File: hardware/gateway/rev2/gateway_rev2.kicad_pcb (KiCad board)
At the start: 2 copper layers, 100 x 45 mm, 80 parts, among them IC1 STM8L151K4T6, IC2 CC1101RGPR, IC3 LT1615ES5-1#TRMPBF, IC4 MIC4427YM, IC5 MB85RC64TAPNF-G-BDERE1, J1 G8250041000YEU, J2 M20-9770342, Q1 IRLML6402TRPBF, U1 2462, Y1 NX3225GA-26.000M-STD-CRG-2

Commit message: EG-59 Schematic with the needed components, plus PCB.
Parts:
- removed ANT1: ANT-433-HESM, MyParts:ANT433HESM
- removed C1, C2: 100nF, Capacitor_SMD:C_0603_1608Metric
- removed C15, C16, C17, C30: 100nF, Capacitor_SMD:C_0402_1005Metric
- removed C18, C19: 12pF, Capacitor_SMD:C_0402_1005Metric
- removed C20, C22: 3.9pF, Capacitor_SMD:C_0402_1005Metric
- removed C21, C25: 220pF, Capacitor_SMD:C_0402_1005Metric
- removed C23: 8.2pF, Capacitor_SMD:C_0402_1005Metric
- removed C24: 5.6pF, Capacitor_SMD:C_0402_1005Metric
- removed C26: 22uF, 6.3V, Capacitor_SMD:C_1206_3216Metric
- removed C27: 4.7pF, Capacitor_SMD:C_0402_1005Metric
- removed C28, C29: 4.7uF, 25V, Capacitor_SMD:C_0805_2012Metric
- removed C6: 47uF, 6.3V, Capacitor_SMD:C_1206_3216Metric
- removed D1: MBR0520LT3G, MyParts:SOD3716X135N
- removed IC3: LT1615ES5-1#TRMPBF, MyParts:SOT95P280X100-5N
- removed IC4: MIC4427YM, MyParts:SOIC127P599X173-8N
- removed J1: G8250041000YEU, MyParts:HDRV4W55P0X200_1X4_800X200X635P
- removed L1, L2, L4: 27nH, Inductor_SMD:L_0402_1005Metric
- removed L3: 22nH, Inductor_SMD:L_0402_1005Metric
- removed L5: CD43NP-100MC, MyParts:CD43NP100MC
- removed Q1: IRLML6402TRPBF, MyParts:SOT95P237X112-3N
- removed R1, R15, R3: 100K, Resistor_SMD:R_0603_1608Metric
- removed R13: 56K, Resistor_SMD:R_0402_1005Metric
- removed R16: 130K, Resistor_SMD:R_0402_1005Metric
- removed R17: 1.15M, Resistor_SMD:R_0402_1005Metric
- removed R2, R5: 1M, Resistor_SMD:R_0603_1608Metric
- removed R4: 10K, Resistor_SMD:R_0603_1608Metric
- removed R6: 510K, Resistor_SMD:R_0603_1608Metric
- removed R7: 1K, Resistor_SMD:R_0603_1608Metric
- removed S1: MASM-14R-8-10, MyParts:MASM14R810
- removed S2: TL6120DF160QG, MyParts:TL6120DF160QG
- added C101: 15pF, Capacitor_SMD:C_0402_1005Metric, F.Cu at (239.9, 118.8)
- added C121: 1pF, Capacitor_SMD:C_0402_1005Metric, F.Cu at (239.9, 120.8)
- added C122: 1.5pF, Capacitor_SMD:C_0402_1005Metric, F.Cu at (239.9, 122.8)
- added C123: 3.3pF, Capacitor_SMD:C_0402_1005Metric, F.Cu at (239.9, 124.8)
- added C124: 100pF, Capacitor_SMD:C_0402_1005Metric, F.Cu at (242.7, 114.9)
- added C125: 12pF, Capacitor_SMD:C_0402_1005Metric, F.Cu at (242.7, 116.9)
- added C131: 1.5pF, Capacitor_SMD:C_0402_1005Metric, F.Cu at (242.7, 118.8)
- added C51: 100nF, Capacitor_SMD:C_0402_1005Metric, F.Cu at (239.9, 114.9)
- added C81: 15pF, Capacitor_SMD:C_0402_1005Metric, F.Cu at (239.9, 116.9)
- added CLK1: SPI_CK, TestPoint:TestPoint_Pad_D1.0mm, F.Cu at (220.1, 111.0)
- added CS1: SPI_CS, TestPoint:TestPoint_Pad_D1.0mm, F.Cu at (220.1, 114.0)
- added GD1: GD0, TestPoint:TestPoint_Pad_D1.0mm, F.Cu at (220.1, 117.1)
- added L121: 12nH, Inductor_SMD:L_0402_1005Metric, F.Cu at (234.1, 114.9)
- added L122: 18nH, Inductor_SMD:L_0402_1005Metric, F.Cu at (234.1, 116.9)
- added L123: 12nH, Inductor_SMD:L_0402_1005Metric, F.Cu at (234.1, 118.9)
- added L124: 12nH, Inductor_SMD:L_0402_1005Metric, F.Cu at (234.1, 120.9)
- added L131: 12nH, Inductor_SMD:L_0402_1005Metric, F.Cu at (234.1, 122.9)
- added L132: 18nH, Inductor_SMD:L_0402_1005Metric, F.Cu at (234.1, 124.9)
- added LED_B1: LED, TestPoint:TestPoint_Pad_D1.0mm, F.Cu at (223.2, 111.0)
- added LED_R1: LED, TestPoint:TestPoint_Pad_D1.0mm, F.Cu at (223.2, 114.0)
- added LED_Y1: LED, TestPoint:TestPoint_Pad_D1.0mm, F.Cu at (223.2, 117.1)
- added MCUVDD1: MCU_VDD, TestPoint:TestPoint_Pad_D1.0mm, F.Cu at (226.2, 111.0)
- added MISO1: SPI_MISO, TestPoint:TestPoint_Pad_D1.0mm, F.Cu at (226.2, 114.0)
- added MOSI1: SPI_MOSI, TestPoint:TestPoint_Pad_D1.0mm, F.Cu at (226.2, 117.1)
- added R171: 56K, Resistor_SMD:R_0402_1005Metric, F.Cu at (234.1, 126.9)
- added RFVDD1: RF_VDD, TestPoint:TestPoint_Pad_D1.0mm, F.Cu at (245.7, 124.3)
- C13: value 1uF -> 100nF
- C9: value 47uF, 6.3V -> 100nF; footprint Capacitor_SMD:C_1206_3216Metric -> Capacitor_SMD:C_0402_1005Metric
- R18, R19: value 33R -> 100R
- R20: value 1M -> 10K
- U1: value 2462 -> IRM-01-3.3; footprint MyParts:2462 -> MyParts:IRM-01-3-3; moved to F.Cu
- Y1: value NX3225GA-26.000M-STD-CRG-2 -> NX3225GA-26MHZ-TI
- moved FID2 84.5 mm to (241.0, 91.0)
- moved H2 82.1 mm to (235.9, 95.5)
- moved FID1 64.3 mm to (241.0, 87.5)
- moved H4 63.8 mm to (235.9, 108.6)
- moved C4 62.7 mm to (224.6, 87.0), turned to 0 degrees
- moved FID3 61.8 mm to (241.0, 94.6)
- moved H1 61.0 mm to (235.9, 89.0)
- moved C5 60.8 mm to (224.6, 89.5), turned to 0 degrees
- moved U1 59.2 mm to (191.5, 154.5)
- moved LS1 54.5 mm to (251.6, 146.1), turned to 0 degrees
- moved R18 51.4 mm to (228.7, 92.0)
- moved R10 50.7 mm to (224.6, 97.0)
- moved LED3 48.3 mm to (225.4, 101.4)
- moved R9 47.6 mm to (224.6, 94.5)
- moved R20 44.9 mm to (228.7, 97.0), turned to 0 degrees
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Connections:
- C11 pad 1: Net-(IC2-DCOUPL) -> RF_VDD
- C9 pad 1: VDD -> RF_VDD
- FB1 pad 1: VDD -> RF_VDD
- FB1 pad 2: RF_VDD -> VDD
- IC1 pad 11: /Buzzer/BZR_P -> BZR_P
- IC1 pad 22: DOOR -> unconnected-(IC1-PD5-Pad22)
- IC1 pad 24: /Buzzer/BZR_N -> BZR_N
- IC1 pad 29: /Buzzer/BZR_EN -> unconnected-(IC1-PC4-Pad29)
- IC1 pad 6: V_MEAS -> unconnected-(IC1-PA6-Pad6)
- J2 pad 1: TX -> GND
- J2 pad 3: GND -> TX
- R18 pad 2: Net-(IC4-OUTA) -> BZR_P
- R19 pad 2: Net-(IC4-OUTB) -> BZR_N
- U1 pad 1: BAT_IN -> unconnected-(U1-AC/L-Pad1)
- Y1 pad 2: GND -> unconnected-(Y1-NC/GND_1-Pad2)
- Y1 pad 4: GND -> unconnected-(Y1-NC/GND_2-Pad4)
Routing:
- net VDD: track 157.1 -> 0.00 mm, vias 5 -> 0
- net GND: track 80.1 -> 0.00 mm, vias 287 -> 0
- net /Buzzer/BZR_EN: track 47.7 -> 0.00 mm, vias 2 -> 0
- net RF_VDD: track 47.6 -> 0.00 mm, vias 4 -> 0
- net /MCU/SDI: track 45.8 -> 0.00 mm, vias 4 -> 0
- net /MCU/SDO: track 40.2 -> 0.00 mm, vias 4 -> 0
- net RX: track 39.2 -> 0.00 mm, vias 1 -> 0
- net /MCU/SCLK: track 36.0 -> 0.00 mm, vias 4 -> 0
- net TX: track 35.8 -> 0.00 mm, vias 2 -> 0
- net +12V: track 34.3 -> 0.00 mm, vias 2 -> 0
- net SCL: track 33.5 -> 0.00 mm, vias 2 -> 0
- net SDA: track 32.1 -> 0.00 mm, vias 2 -> 0
- net /MCU/CS: track 31.4 -> 0.00 mm, vias 2 -> 0
- net /MCU/IRQ: track 30.5 -> 0.00 mm, vias 2 -> 0
- net LED_B: track 28.9 -> 0.00 mm, vias 2 -> 0
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- removed copper zone on B.Cu, net GND
- removed copper zone on F.Cu, net GND
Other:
- board size 100 x 45 mm -> 94 x 78 mm
- board text removed: "Exit Guardian - Gateway REV1.0 NPX4U 2025"

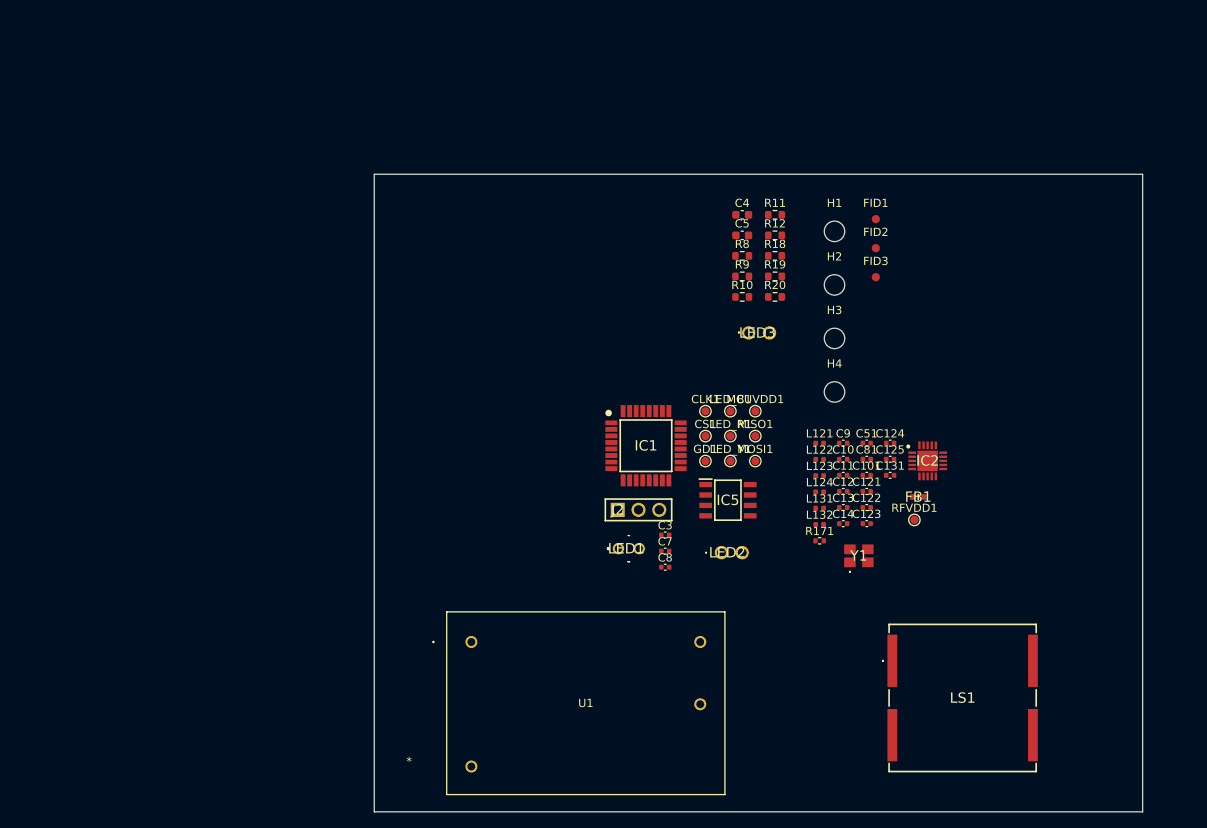
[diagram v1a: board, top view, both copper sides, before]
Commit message: EG-59 First mechanical project with the AC-DC component and buzzer.
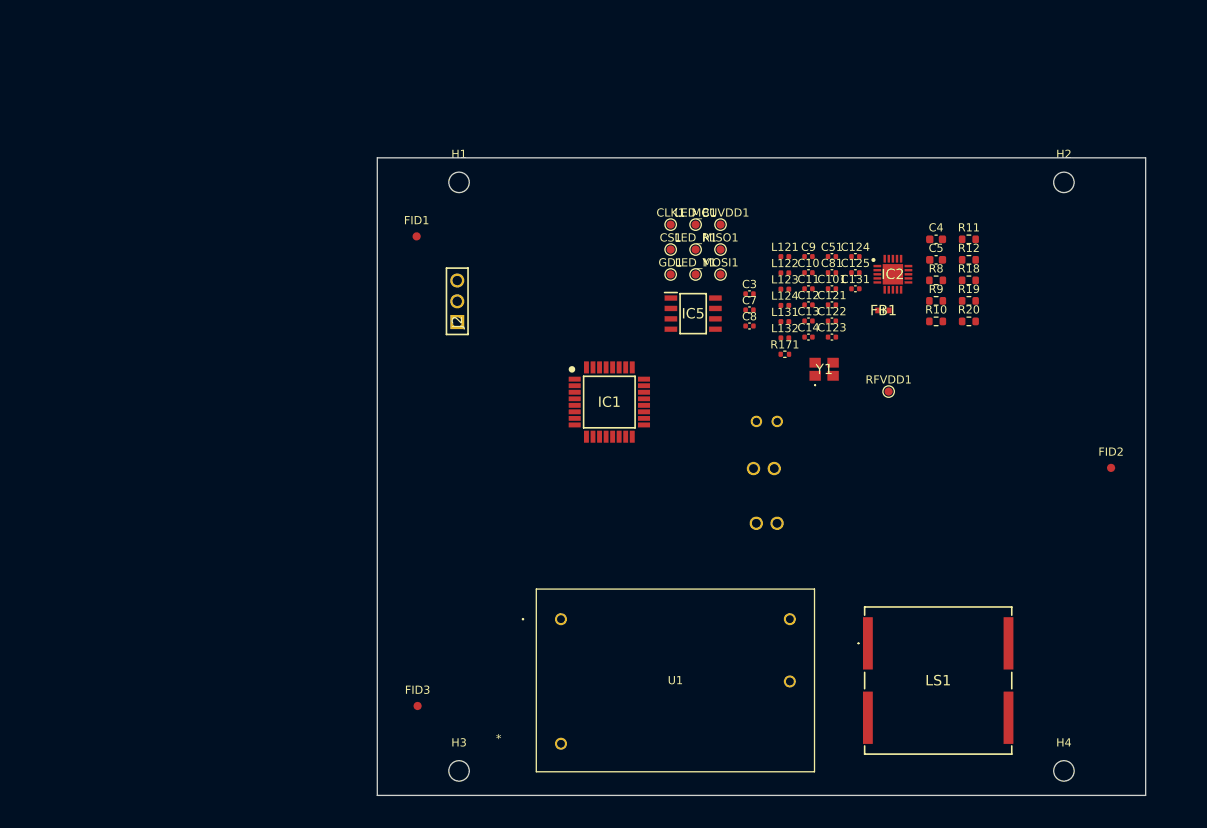
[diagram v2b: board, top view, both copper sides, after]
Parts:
- LED1, LED2, LED3: moved to B.Cu
- moved FID3 76.8 mm to (184.9, 147.1)
- moved H3 70.1 mm to (190.0, 155.0)
- moved FID1 56.2 mm to (184.8, 89.6)
- moved H4 54.2 mm to (264.0, 155.0)
- moved H1 46.3 mm to (190.0, 83.0)
- moved FID2 39.4 mm to (269.8, 117.9)
- moved C7 31.3 mm to (225.5, 98.6)
- moved C8 31.3 mm to (225.5, 100.6)
- moved C3 31.3 mm to (225.5, 96.6)
- moved H2 30.7 mm to (264.0, 83.0)
- moved J2 30.2 mm to (189.8, 100.1), turned to 90 degrees
- moved LED1 24.9 mm to (228.9, 112.2), turned to 180 degrees
- moved C4 23.9 mm to (248.4, 90.0)
- moved C5 23.9 mm to (248.4, 92.5)
- moved R10 23.9 mm to (248.4, 100.0)
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
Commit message: EG-59 Correct position of AC-DC and buzzer in the PCB.
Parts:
- added TP1: TestPoint, TestPoint:TestPoint_Plated_Hole_D2.0mm, F.Cu at (190.0, 133.0)
- added TP2: TestPoint, TestPoint:TestPoint_Plated_Hole_D2.0mm, F.Cu at (190.0, 147.0)
- moved FID1 13.5 mm to (196.5, 83.0)
- moved FID3 8.03 mm to (183.6, 155.0)
- moved LS1 4.13 mm to (249.9, 140.0), turned to 90 degrees
- moved U1 3.93 mm to (201.9, 147.8)
- moved FID2 2.29 mm to (270.8, 120.0)
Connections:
- U1 pad 1: unconnected-(U1-AC/L-Pad1) -> Net-(U1-AC/L)
- U1 pad 12: unconnected-(U1-+VO-Pad12) -> VDD
- U1 pad 13: unconnected-(U1--VO-Pad13) -> GND
- U1 pad 24: unconnected-(U1-AC/N-Pad24) -> Net-(U1-AC/N)
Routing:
- net Net-(U1-AC/L): track 0.00 -> 12.2 mm
- net Net-(U1-AC/N): track 0.00 -> 12.1 mm
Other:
- board text added: "Exit Guardian - Gateway REV2.0 NPX4U 2026"

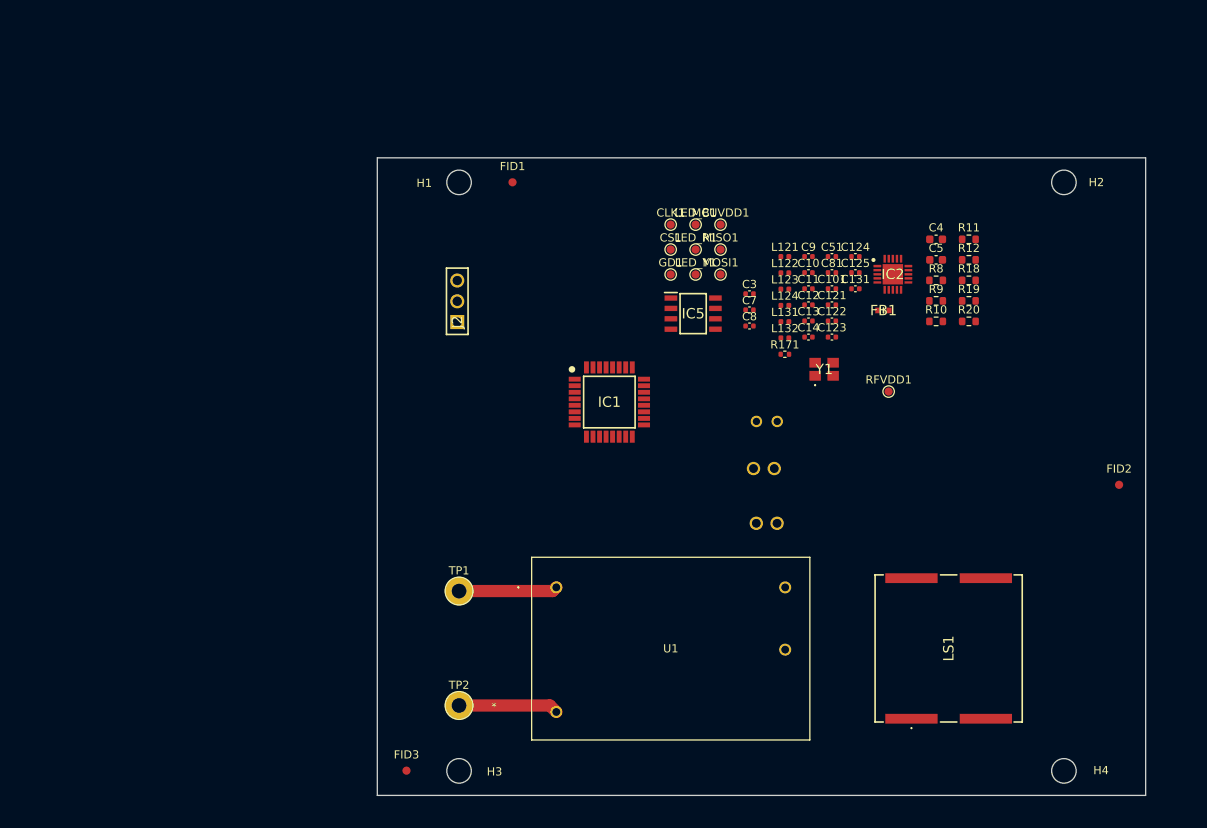
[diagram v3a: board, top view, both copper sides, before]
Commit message: EG-59 Antenna and headers fix, from schematic to 3D.
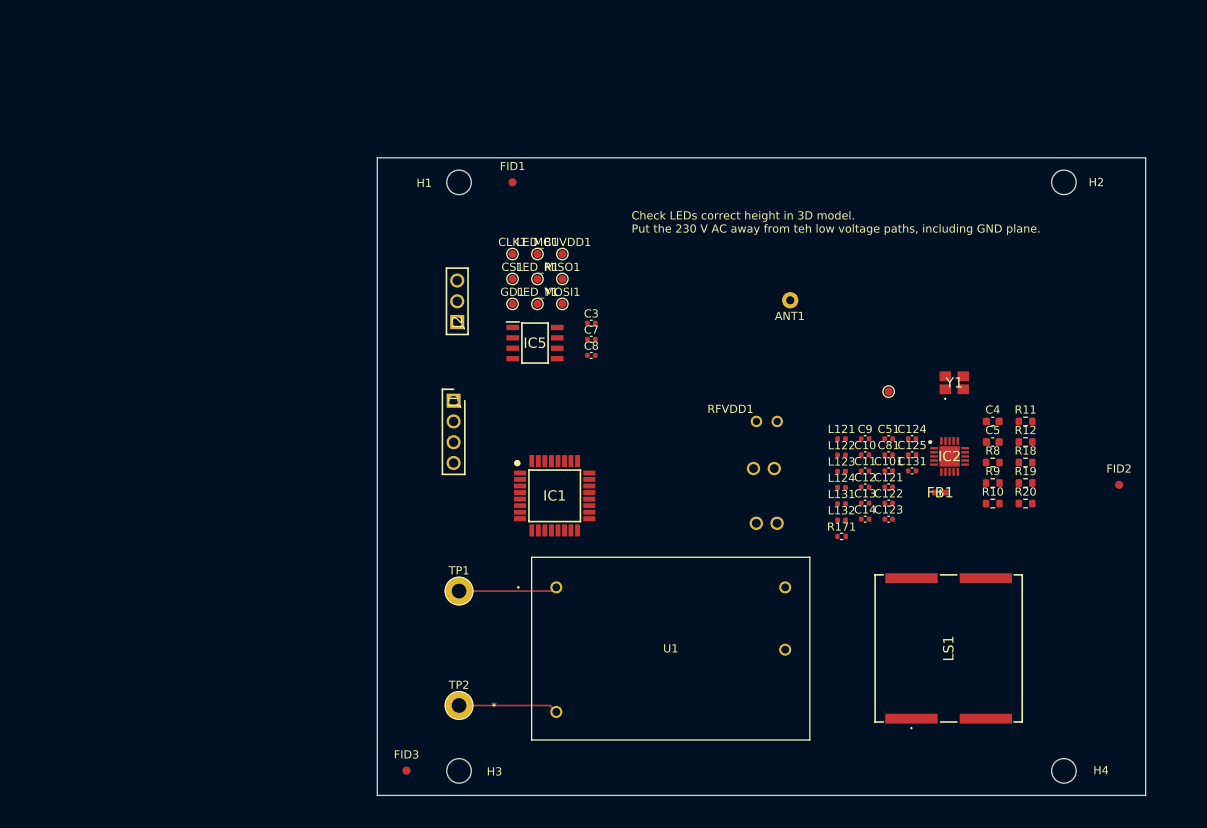
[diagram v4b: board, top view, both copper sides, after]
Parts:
- added ANT1: ~, MyParts:Antenna_hole, F.Cu at (230.4, 99.2)
- added J1: 22-28-4044, MyParts:HDRV4W66P0X254_1X4_1016X249X1067P, F.Cu at (189.3, 109.7)
- moved C101 23.3 mm to (242.6, 118.3)
- moved C11 23.3 mm to (239.7, 118.3)
- moved C12 23.3 mm to (239.7, 120.3)
- moved C121 23.3 mm to (242.6, 120.3)
- moved C122 23.3 mm to (242.6, 122.2)
- moved C13 23.3 mm to (239.7, 122.2)
- moved C131 23.3 mm to (245.4, 118.3)
- moved R18 23.3 mm to (259.3, 117.3)
- moved R8 23.3 mm to (255.3, 117.3)
- moved L123 23.3 mm to (236.8, 118.4)
- moved C10 23.3 mm to (239.7, 116.3)
- moved C123 23.3 mm to (242.6, 124.2)
- moved C124 23.3 mm to (245.4, 114.4)
- moved C125 23.3 mm to (245.4, 116.3)
- moved C14 23.3 mm to (239.7, 124.2)
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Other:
- board text added: "Check LEDs correct height in 3D model. Put the 230 V AC away from teh low voltage paths, including GND plane."

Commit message: EG-59 Schematic finished.
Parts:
- removed TP1, TP2: TestPoint, TestPoint:TestPoint_Plated_Hole_D2.0mm
- added J_L1: ~, MyParts:230V, F.Cu at (190.9, 148.0)
- added J_N1: ~, MyParts:230V, F.Cu at (190.4, 132.9)
- added S1: TS02-66-100-BK-160-SCR-D, MyParts:TS0266100BK100LCRD, B.Cu at (235.3, 110.8)
- moved L121 19.2 mm to (246.2, 97.7)
- moved L123 19.2 mm to (246.2, 101.6)
- moved L124 19.2 mm to (246.2, 103.6)
- moved L132 19.2 mm to (246.2, 107.6)
- moved R171 19.2 mm to (246.2, 109.6)
- moved L122 19.2 mm to (246.2, 99.7)
- moved L131 19.2 mm to (246.2, 105.6)
- moved Y1 19.2 mm to (260.0, 90.8)
- moved C101 19.2 mm to (252.0, 101.6)
- moved C11 19.2 mm to (249.1, 101.6)
- moved C12 19.2 mm to (249.1, 103.6)
- moved C121 19.2 mm to (252.0, 103.6)
- moved C122 19.2 mm to (252.0, 105.5)
- moved C123 19.2 mm to (252.0, 107.5)
- moved C13 19.2 mm to (249.1, 105.5)
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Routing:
- net Net-(J_L1-V): track 12.2 -> 0.00 mm
- net Net-(J_N1-V): track 12.1 -> 0.64 mm
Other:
- board text added: "Check LEDs correct height in 3D model. Put the 230 V AC away from the low voltage paths, including GND plane."
- board text removed: "Check LEDs correct height in 3D model. Put the 230 V AC away from teh low voltage paths, including GND plane."
